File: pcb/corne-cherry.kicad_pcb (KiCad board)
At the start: 2 copper layers, 275.5 x 105.6 mm, 168 parts, among them J1 MJ-4PP-9, J2 OLED, J3 MJ-4PP-9, J4 OLED, J5 Conn_01x01_Male, J6 Conn_01x01_Male, P1 Conn_01x03, P3 Conn_01x03, SW1 SW_PUSH, SW10 SW_PUSH, SW11 SW_PUSH, SW12 SW_PUSH, SW13 SW_PUSH, SW14 SW_PUSH, SW15 SW_PUSH, SW16 SW_PUSH, SW17 SW_PUSH, SW18 SW_PUSH, SW19 SW_PUSH, SW2 SW_PUSH, SW20 SW_PUSH, SW21 SW_PUSH, SW22 SW_PUSH, SW23 SW_PUSH, SW24 SW_PUSH, SW25 SW_PUSH, SW26 SW_PUSH, SW27 SW_PUSH, SW28 SW_PUSH, SW29 SW_PUSH, SW3 SW_PUSH, SW30 SW_PUSH, SW31 SW_PUSH, SW32 SW_PUSH, SW33 SW_PUSH, SW34 SW_PUSH, SW35 SW_PUSH, SW36 SW_PUSH, SW37 SW_PUSH, SW38 SW_PUSH, SW39 SW_PUSH, SW4 SW_PUSH, SW40 SW_PUSH, SW41 SW_PUSH, SW42 SW_PUSH, SW5 SW_PUSH, SW6 SW_PUSH, SW7 SW_PUSH, SW8 SW_PUSH, SW9 SW_PUSH, U1 ProMicro, U2 ProMicro

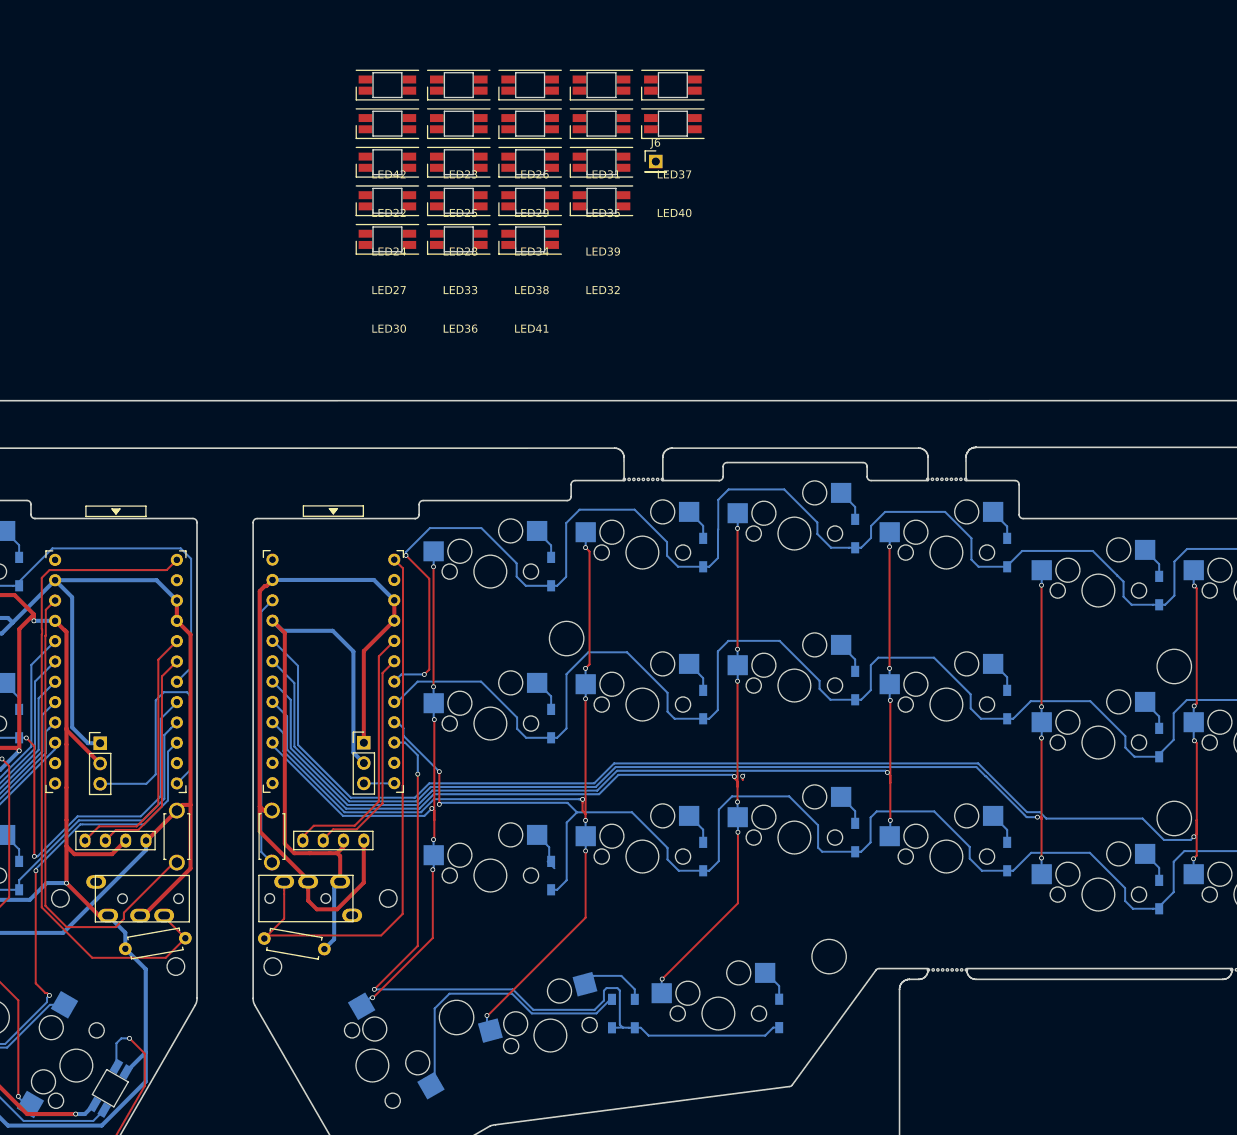
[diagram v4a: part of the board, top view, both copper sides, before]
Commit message: Finish left half rgb with jumpers
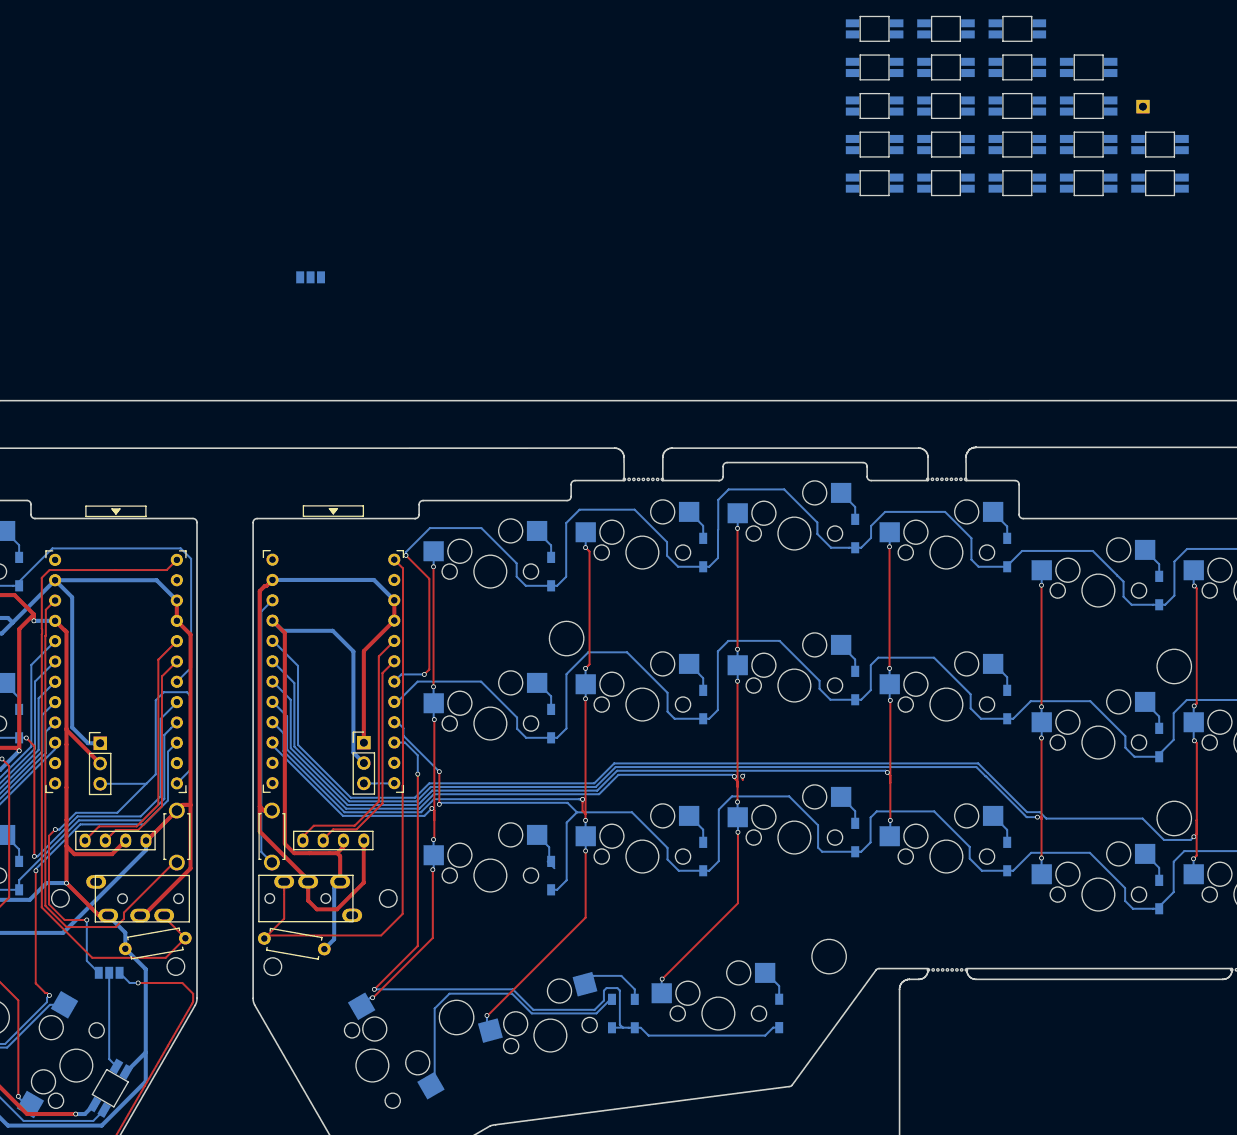
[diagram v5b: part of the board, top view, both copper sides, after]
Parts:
- added JP1: SolderJumper_3_Open, Jumper:SolderJumper-3_P1.3mm_Open_Pad1.0x1.5mm, B.Cu at (134.0, 83.6)
- added JP2: SolderJumper_3_Open, Jumper:SolderJumper-3_P1.3mm_Open_Pad1.0x1.5mm, B.Cu at (159.1, -3.37)
- J6, LED22, LED23, LED24, LED25, LED26, LED27, LED28, LED29, LED30, LED31, LED32, LED33, LED34, LED35, LED36, LED37, LED38, LED39, LED40, LED41, LED42: moved to B.Cu
- moved LED30 66.3 mm to (229.6, -34.4)
- moved LED36 66.3 mm to (238.6, -34.4)
- moved LED41 66.3 mm to (247.5, -34.4)
- moved LED32 63.1 mm to (256.4, -29.6)
- moved LED27 63.1 mm to (229.6, -29.6)
- moved LED33 63.1 mm to (238.6, -29.6)
- moved LED38 63.1 mm to (247.5, -29.6)
- moved LED31 62.1 mm to (256.4, -15.2)
- moved LED23 62.1 mm to (238.6, -15.2)
- moved LED26 62.1 mm to (247.5, -15.2)
- moved LED42 62.1 mm to (229.6, -15.2)
- moved LED37 62.1 mm to (265.3, -15.2)
- moved LED39 61.3 mm to (256.4, -24.8)
- moved LED24 61.3 mm to (229.6, -24.8)
- moved LED28 61.3 mm to (238.6, -24.8)
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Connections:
- LED21 pad 4: Net-(J5-Pad1) -> Net-(JP1-Pad2)
- LED33 pad 4: Net-(J6-Pad1) -> Net-(JP2-Pad2)
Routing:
- net LED: track 33.2 -> 69.4 mm, vias 0 -> 2
- net Net-(JP1-Pad2): track 0.00 -> 12.1 mm
- net Net-(J5-Pad1): track 110.2 -> 122.1 mm

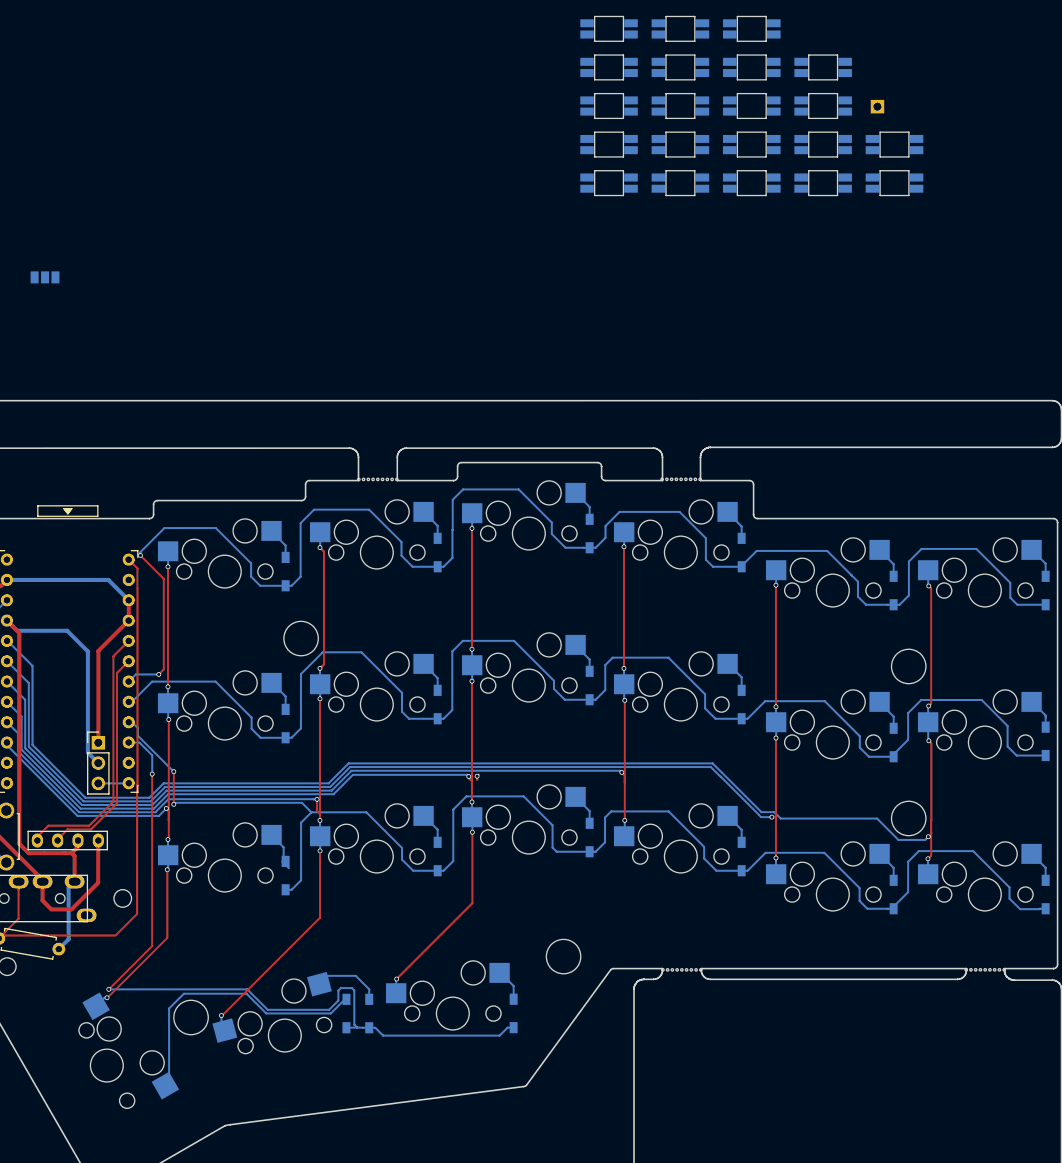
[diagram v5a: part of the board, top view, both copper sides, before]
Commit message: Place RGB
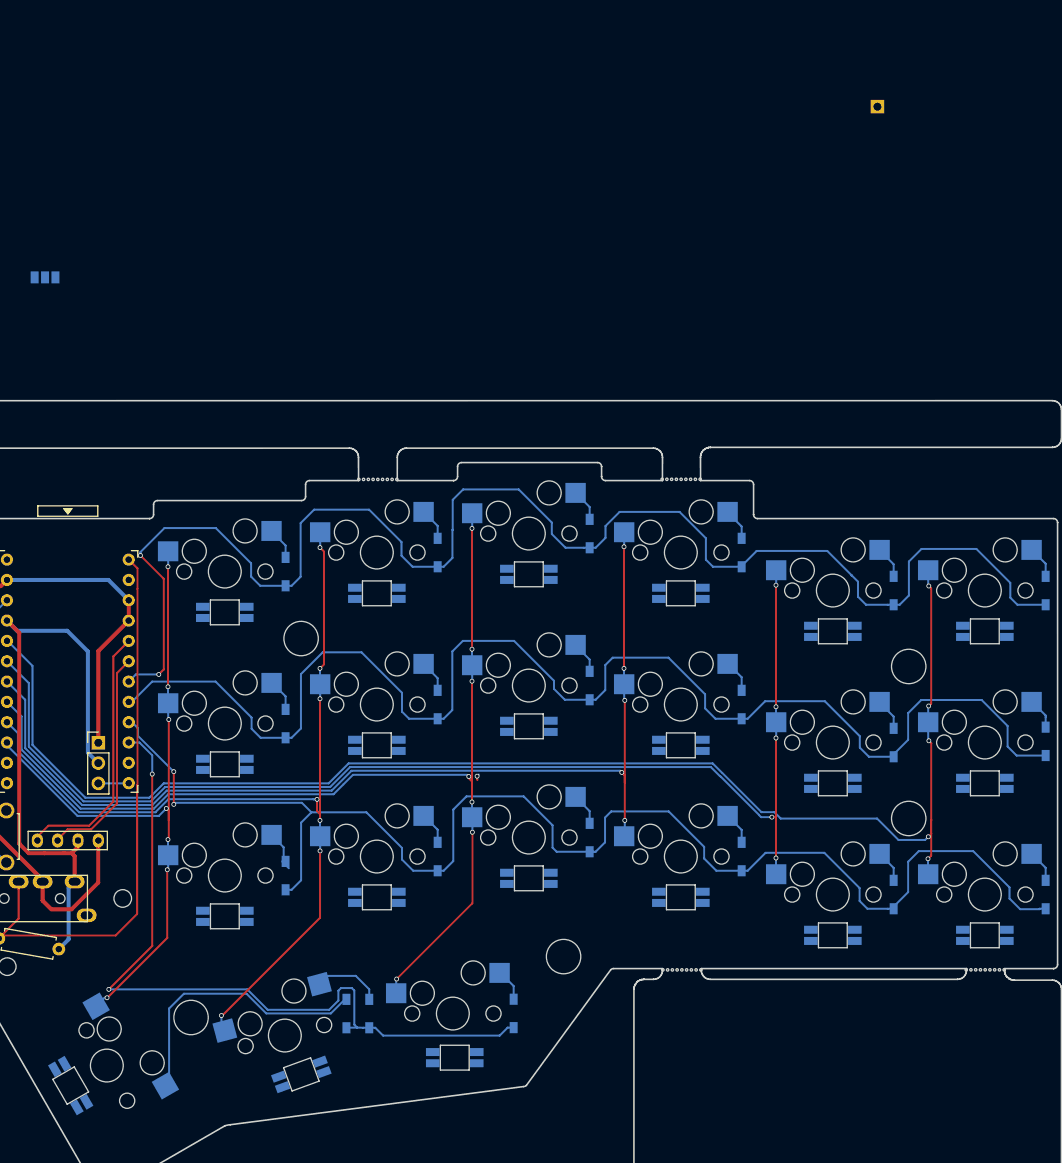
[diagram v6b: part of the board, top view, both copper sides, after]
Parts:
- moved LED25 140.2 mm to (162.3, 97.7), turned to 120 degrees
- moved LED29 129.2 mm to (191.2, 96.3), turned to 200 degrees
- moved LED33 127.0 mm to (210.4, 94.2), turned to 180 degrees
- moved LED24 112.1 mm to (181.6, 76.5)
- moved LED36 108.6 mm to (238.6, 74.1)
- moved LED32 107.8 mm to (219.6, 71.8)
- moved LED28 105.9 mm to (200.6, 74.1)
- moved LED42 105.1 mm to (276.6, 78.9)
- moved LED39 103.7 mm to (257.6, 78.9)
- moved LED41 98.7 mm to (276.6, 59.9), turned to 180 degrees
- moved LED23 92.3 mm to (181.6, 57.5), turned to 180 degrees
- moved LED38 90.1 mm to (257.6, 59.9), turned to 180 degrees
- moved LED27 89.6 mm to (200.6, 55.1), turned to 180 degrees
- moved LED31 77.2 mm to (219.6, 52.8), turned to 180 degrees
- moved LED35 77.2 mm to (238.6, 55.1), turned to 180 degrees
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
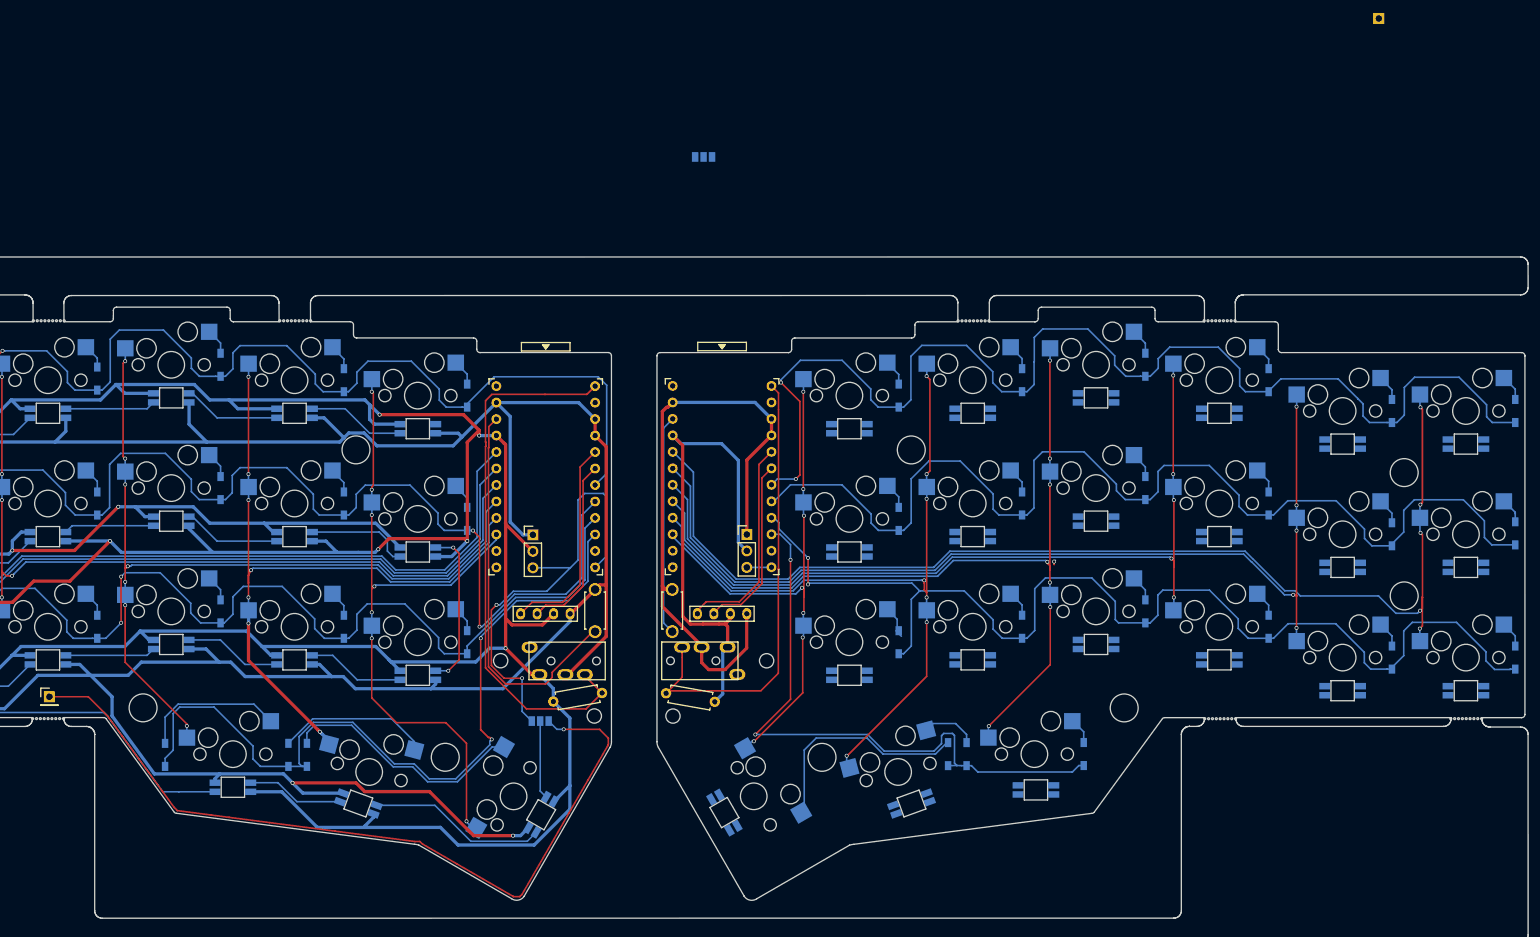
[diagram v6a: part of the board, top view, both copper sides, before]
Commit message: Finish RGB on right half
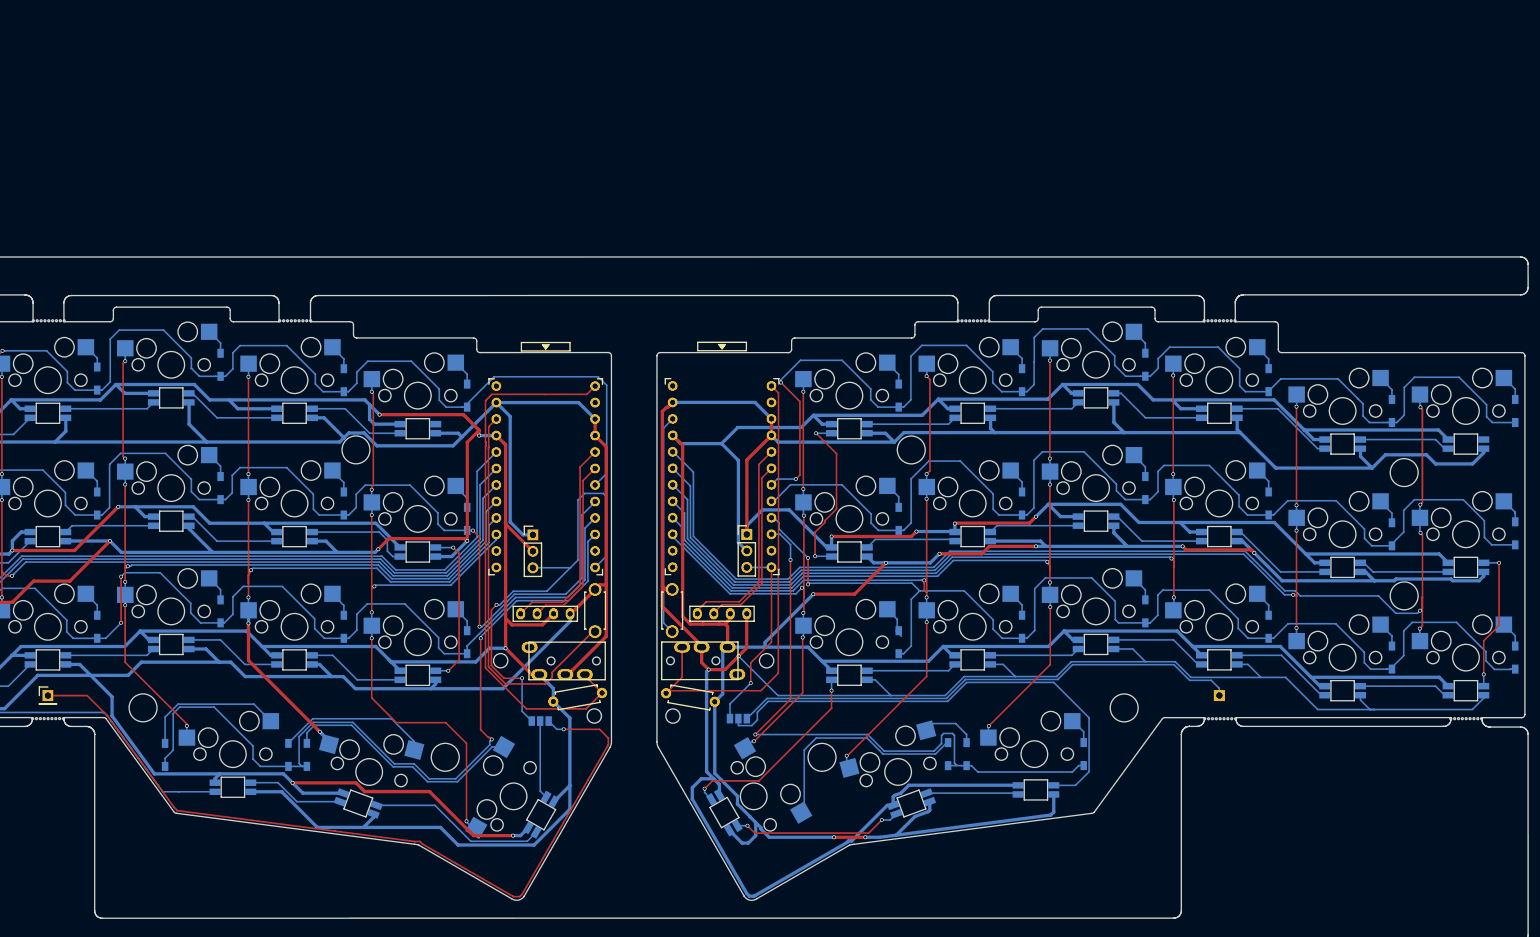
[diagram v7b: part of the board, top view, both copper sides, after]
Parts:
- moved J6 107.2 mm to (238.6, 79.6)
- moved JP2 86.7 mm to (164.5, 83.2)
- moved J5 0.29 mm to (58.1, 79.6)
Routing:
- net GNDA: track 94.9 -> 601.4 mm, vias 0 -> 6
- net VDD: track 77.0 -> 573.5 mm, vias 0 -> 8
- net Net-(J6-Pad1): track 0.00 -> 78.9 mm
- net Net-(JP2-Pad2): track 0.00 -> 75.4 mm
- net Net-(LED24-Pad4): track 0.00 -> 31.2 mm, vias 0 -> 2
- net Net-(LED22-Pad4): track 0.00 -> 26.6 mm, vias 0 -> 2
- net Net-(LED25-Pad4): track 0.00 -> 26.2 mm, vias 0 -> 2
- net LED_r: track 3.81 -> 29.8 mm, vias 0 -> 1
- net Net-(LED41-Pad4): track 0.00 -> 22.3 mm, vias 0 -> 2
- net Net-(LED35-Pad4): track 0.00 -> 16.0 mm
- net Net-(LED36-Pad2): track 0.00 -> 16.0 mm
- net Net-(LED34-Pad2): track 0.00 -> 16.0 mm
- net Net-(LED31-Pad4): track 0.00 -> 15.1 mm
- net Net-(LED32-Pad2): track 0.00 -> 15.1 mm
- net Net-(LED30-Pad2): track 0.00 -> 15.1 mm
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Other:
- board text added: "https://github.com/ItsWaffIe/waffle_corne"
- board text removed: "https://github.com/wafflekeebs/waffle_corne"

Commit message: Add silkscreen stuff
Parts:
- removed the G*** at (134.0, 47.0)
- added G***: LOGO, weeb:dots4, F.Cu at (91.1, 32.9)
- added G***: LOGO, weeb:dots4, F.Cu at (48.2, 51.3)
- added G***: LOGO, weeb:ae4, F.Cu at (135.7, 47.5)
- added G***: LOGO, weeb:dots4, F.Cu at (109.5, 88.3)
- added G***: LOGO, weeb:dots4, F.Cu at (48.2, 88.3)
- added G***: LOGO, weeb:dots4, F.Cu at (207.3, 32.8)
- added G***: LOGO, weeb:dots4, F.Cu at (250.2, 88.1)
- added G***: LOGO, weeb:dots4, F.Cu at (188.9, 88.1)
- added G***: LOGO, weeb:dots4, F.Cu at (250.2, 51.3)
- added G***: LOGO, weeb:dots4, F.Cu at (188.9, 51.3)
- added G***: LOGO, weeb:dots4, F.Cu at (109.5, 51.3)
